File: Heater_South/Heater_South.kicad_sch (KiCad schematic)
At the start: 3 parts, among them J1 South_Heater_1, J2 South_Heater_2, J3 Heater South

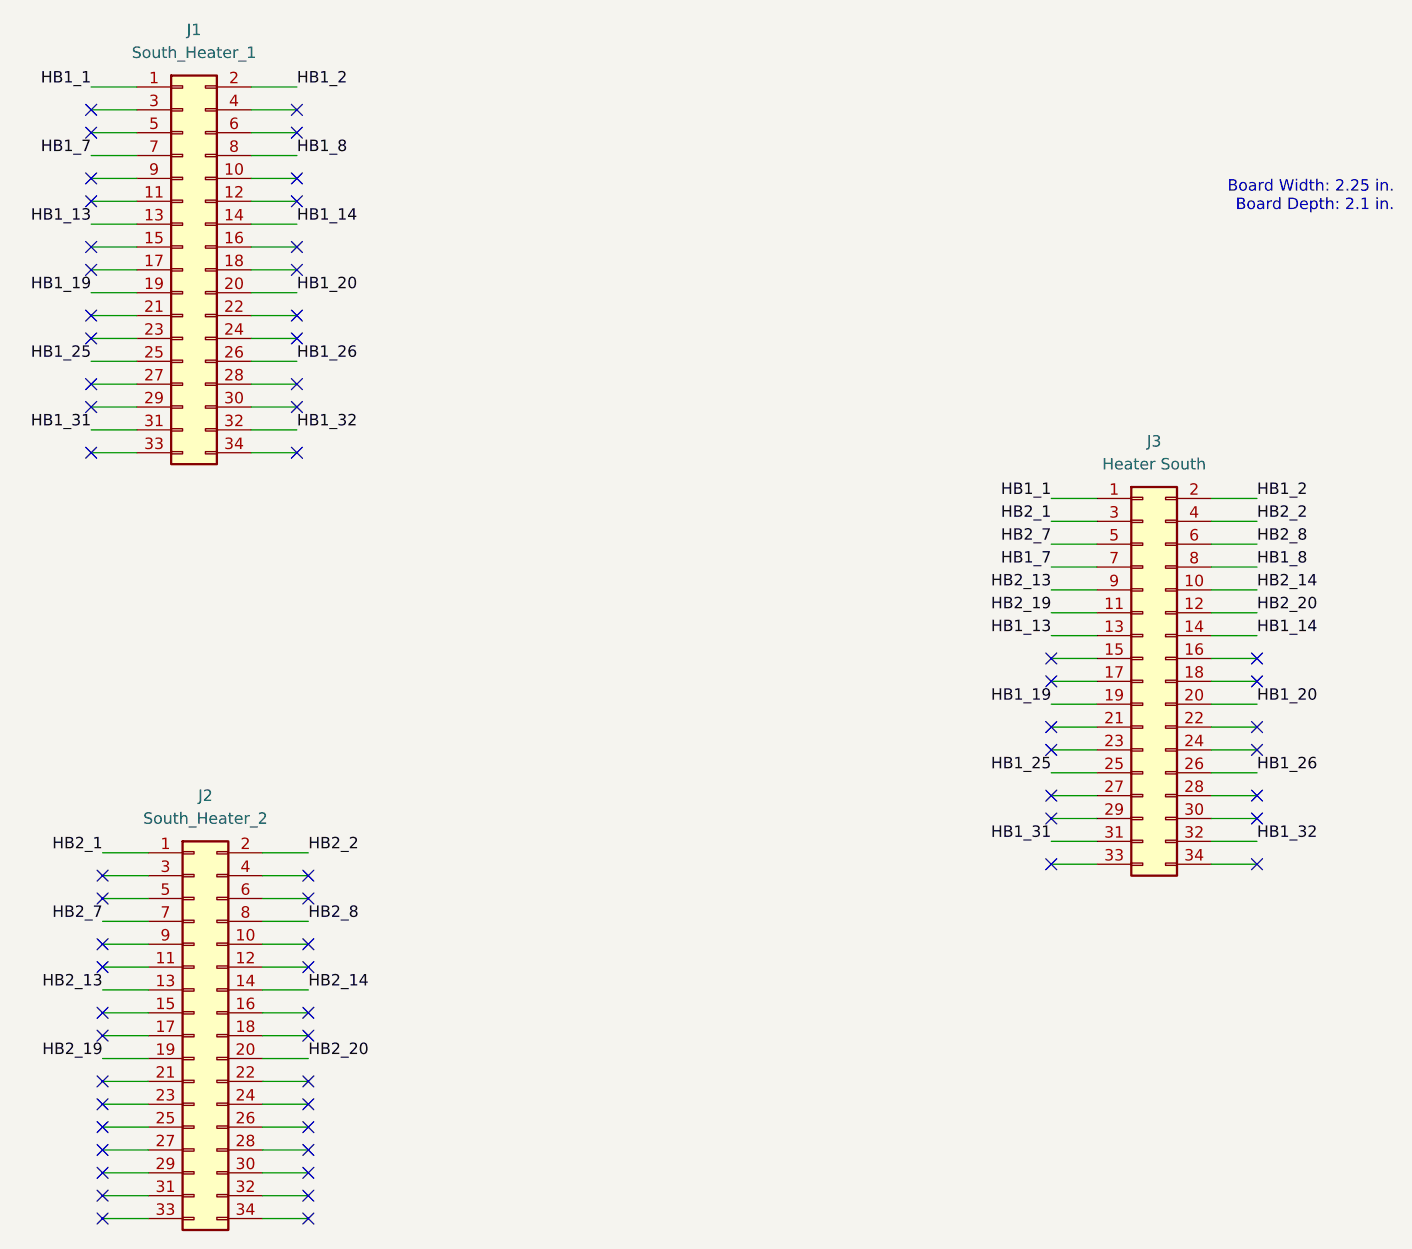
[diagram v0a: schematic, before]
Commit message: Updated Heater South with correct mapping referencing DCT_Heater_Driver schematic. Updated silscreen on all boards. Generated fabrication files.
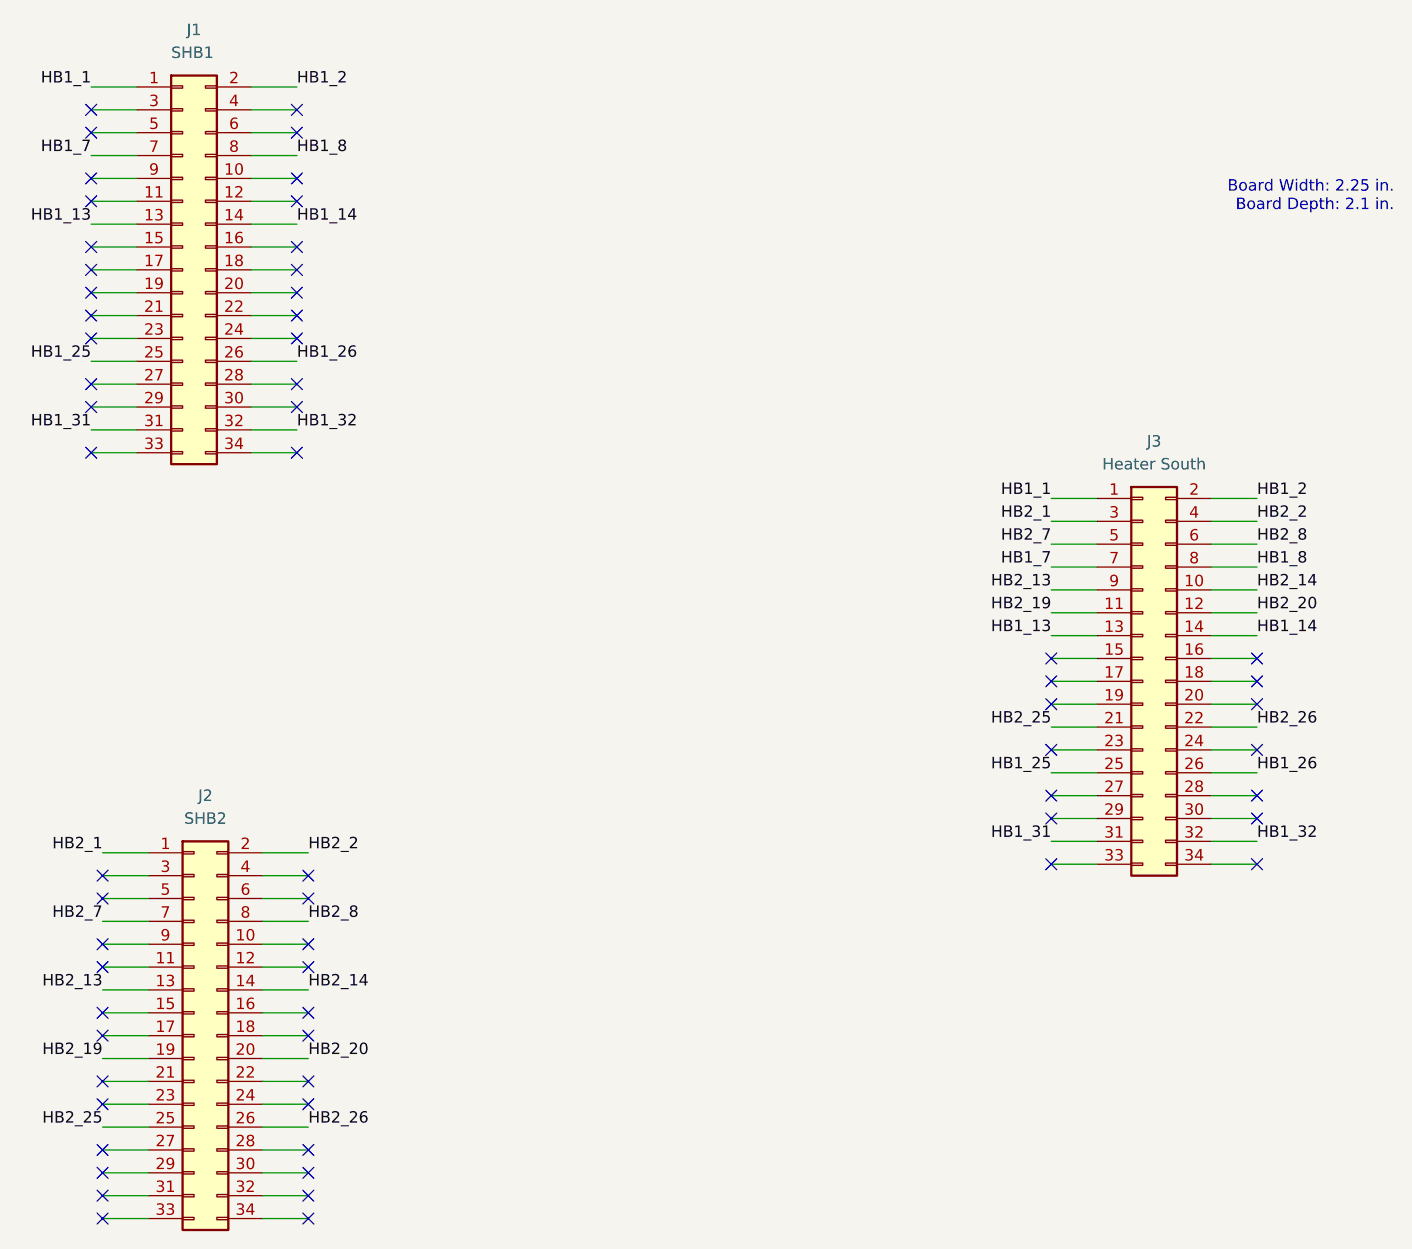
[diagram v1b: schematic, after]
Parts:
- J1: value South_Heater_1 -> SHB1
- J2: value South_Heater_2 -> SHB2
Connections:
- net HB2_25: now reaches J3.21 (Pin_21)
- net HB2_25: now also J2.25 (Pin_25)
- net HB2_26: now reaches J3.22 (Pin_22)
- net HB2_26: now also J2.26 (Pin_26)
- net HB1_19: no longer names the net of J3.19 (Pin_19)
- net HB1_19: no longer J1.19 (Pin_19)
- net HB1_20: no longer names the net of J3.20 (Pin_20)
- net HB1_20: no longer J1.20 (Pin_20)
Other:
- title: Heater Pass Through North -> Heater Pass Through South
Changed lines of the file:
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@@
   (paper "USLetter")
   (title_block
-    (title "Heater Pass Through North")
+    (title "Heater Pass Through South")
     (date "2023-09-09")
     (rev "B")
@@
   (no_connect (at 80.01 152.4))
   (no_connect (at 80.01 154.94))
+  (no_connect (at 185.42 110.49))
   (no_connect (at 78.74 77.47))
   (no_connect (at 185.42 115.57))
@@
   (no_connect (at 208.28 107.95))
   (no_connect (at 101.6 74.93))
+  (no_connect (at 101.6 64.77))
   (no_connect (at 78.74 82.55))
   (no_connect (at 208.28 120.65))
@@
   (no_connect (at 101.6 82.55))
   (no_connect (at 185.42 107.95))
-  (no_connect (at 102.87 157.48))
-  (no_connect (at 80.01 157.48))
   (no_connect (at 208.28 123.19))
   (no_connect (at 101.6 62.23))
-  (no_connect (at 208.28 113.03))
   (no_connect (at 101.6 59.69))
   (no_connect (at 102.87 167.64))
@@
   (no_connect (at 80.01 165.1))
   (no_connect (at 80.01 167.64))
+  (no_connect (at 208.28 110.49))
   (no_connect (at 208.28 128.27))
   (no_connect (at 208.28 105.41))
+  (no_connect (at 78.74 64.77))
   (no_connect (at 101.6 67.31))
   (no_connect (at 185.42 120.65))
@@
   (no_connect (at 101.6 69.85))
   (no_connect (at 78.74 74.93))
-  (no_connect (at 185.42 113.03))
   (no_connect (at 185.42 128.27))
   (no_connect (at 208.28 115.57))
@@
     (effects (font (size 1.27 1.27)) (justify left bottom))
   )
-  (label "HB1_20" (at 101.6 64.77 0) (fields_autoplaced)
-    (effects (font (size 1.27 1.27)) (justify left bottom))
-  )
   (label "HB1_25" (at 185.42 118.11 180) (fields_autoplaced)
     (effects (font (size 1.27 1.27)) (justify right bottom))
@@
     (effects (font (size 1.27 1.27)) (justify right bottom))
   )
+  (label "HB2_26" (at 102.87 157.48 0) (fields_autoplaced)
+    (effects (font (size 1.27 1.27)) (justify left bottom))
+  )
   (label "HB1_32" (at 101.6 80.01 0) (fields_autoplaced)
     (effects (font (size 1.27 1.27)) (justify left bottom))
@@
     (effects (font (size 1.27 1.27)) (justify left bottom))
   )
-  (label "HB1_19" (at 185.42 110.49 180) (fields_autoplaced)
-    (effects (font (size 1.27 1.27)) (justify right bottom))
-  )
-  (label "HB1_19" (at 78.74 64.77 180) (fields_autoplaced)
-    (effects (font (size 1.27 1.27)) (justify right bottom))
-  )
   (label "HB1_31" (at 78.74 80.01 180) (fields_autoplaced)
     (effects (font (size 1.27 1.27)) (justify right bottom))
@@
     (effects (font (size 1.27 1.27)) (justify left bottom))
   )
+  (label "HB2_25" (at 80.01 157.48 180) (fields_autoplaced)
+    (effects (font (size 1.27 1.27)) (justify right bottom))
+  )
   (label "HB1_7" (at 185.42 95.25 180) (fields_autoplaced)
     (effects (font (size 1.27 1.27)) (justify right bottom))
@@
     (effects (font (size 1.27 1.27)) (justify left bottom))
   )
+  (label "HB2_26" (at 208.28 113.03 0) (fields_autoplaced)
+    (effects (font (size 1.27 1.27)) (justify left bottom))
+  )
   (label "HB2_19" (at 80.01 149.86 180) (fields_autoplaced)
     (effects (font (size 1.27 1.27)) (justify right bottom))
   )
+  (label "HB2_25" (at 185.42 113.03 180) (fields_autoplaced)
+    (effects (font (size 1.27 1.27)) (justify right bottom))
+  )
   (label "HB2_8" (at 102.87 134.62 0) (fields_autoplaced)
     (effects (font (size 1.27 1.27)) (justify left bottom))
   )
   (label "HB2_14" (at 208.28 97.79 0) (fields_autoplaced)
-    (effects (font (size 1.27 1.27)) (justify left bottom))
-  )
-  (label "HB1_20" (at 208.28 110.49 0) (fields_autoplaced)
     (effects (font (size 1.27 1.27)) (justify left bottom))
   )
@@
     (pin "9")
     (instances
-      (project "Heater_South_DCT_HSK"
+      (project "Heater_South"
         (path "/b67bdb50-32e2-49f2-b2ed-35caa82406e6"
           (reference "J3") (unit 1)
@@
   )
   (symbol (lib_id "Connector_Generic:Conn_02x17_Odd_Even") (at 88.9 62.23 0) (unit 1)
-    (in_bom yes) (on_board yes) (dnp no) (fields_autoplaced)
+    (in_bom yes) (on_board yes) (dnp no)
     (property "Reference" "J1" (at 90.17 35.56 0)
       (effects (font (size 1.27 1.27)))
     )
-    (property "Value" "South_Heater_1" (at 90.17 38.1 0)
-      (effects (font (size 1.27 1.27)))
+    (property "Value" "SHB1" (at 87.63 38.1 0)
+      (effects (font (size 1.27 1.27)) (justify left))
     )
     (property "Footprint" "HELIX:HELIX_DCT_ICDconnector34pin_corrected" (at 88.9 62.23 0)
@@
     (pin "9")
     (instances
-      (project "Heater_South_DCT_HSK"
+      (project "Heater_South"
         (path "/b67bdb50-32e2-49f2-b2ed-35caa82406e6"
           (reference "J1") (unit 1)
@@
       (effects (font (size 1.27 1.27)))
     )
-    (property "Value" "South_Heater_2" (at 91.44 123.19 0)
+    (property "Value" "SHB2" (at 91.44 123.19 0)
       (effects (font (size 1.27 1.27)))
     )
@@
     (pin "9")
     (instances
-      (project "Heater_South_DCT_HSK"
+      (project "Heater_South"
         (path "/b67bdb50-32e2-49f2-b2ed-35caa82406e6"
           (reference "J2") (unit 1)
